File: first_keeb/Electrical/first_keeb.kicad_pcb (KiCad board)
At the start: 2 copper layers, 91.5 x 64.5 mm, 23 parts, among them U1 RPi_Pico_SMD_TH

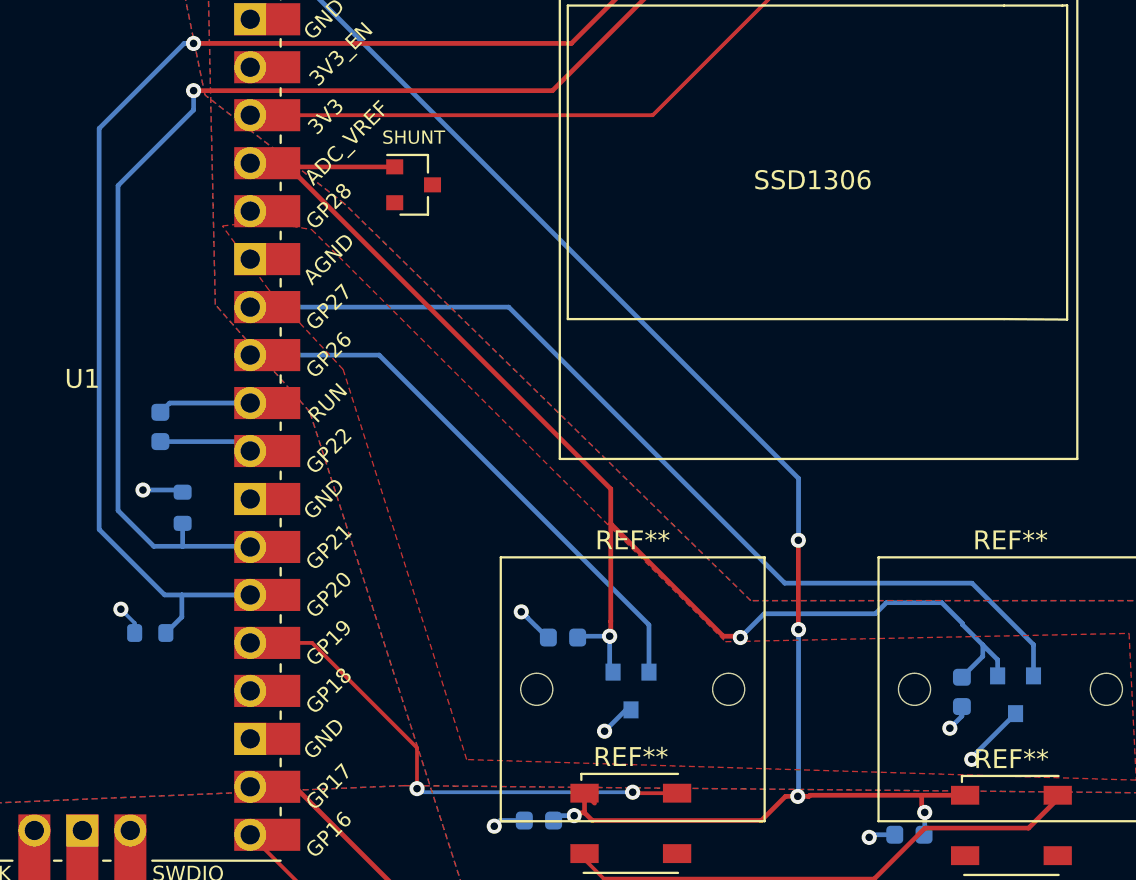
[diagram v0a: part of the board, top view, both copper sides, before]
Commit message: fix ground plane issues
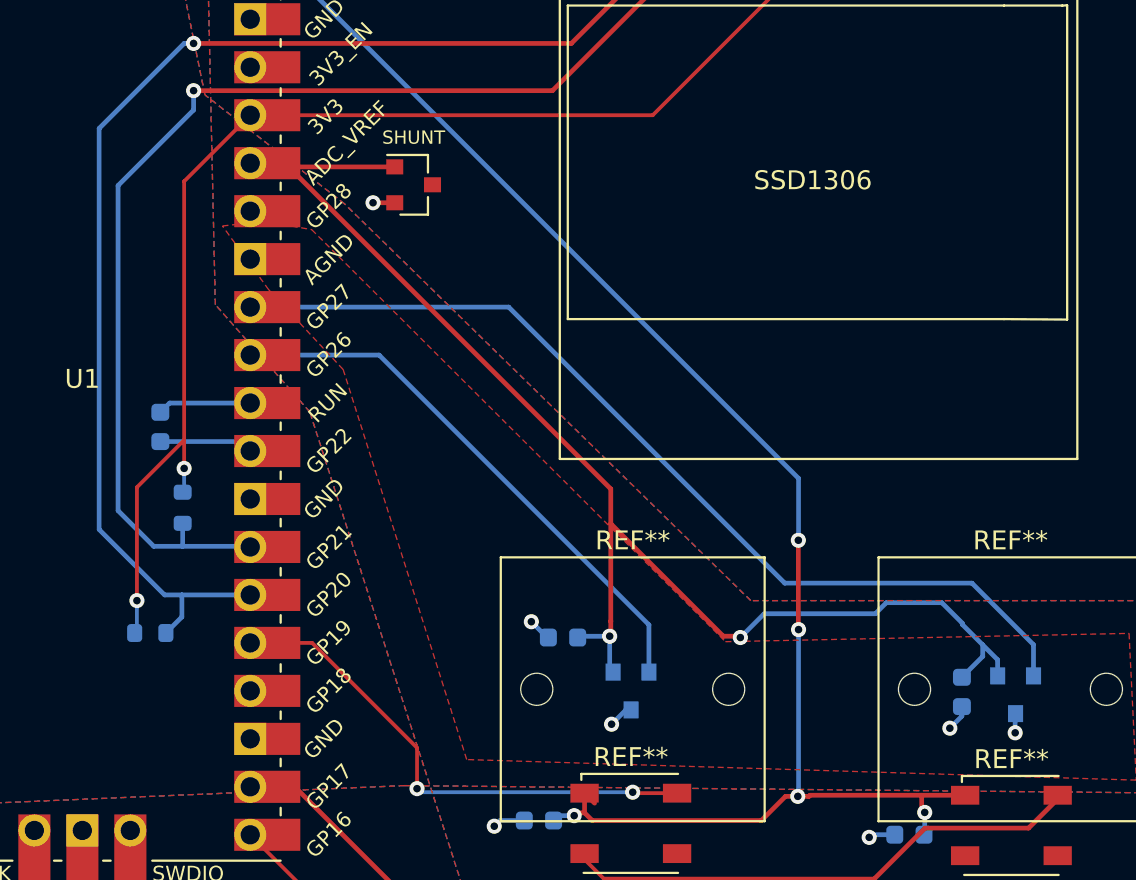
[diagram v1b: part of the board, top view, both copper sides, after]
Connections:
- CUP pad 2: (no net) -> AGND
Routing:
- net (no net): track 559.3 -> 590.6 mm, vias 12 -> 13
- net GND: track 7.09 -> 4.28 mm, vias 4 -> 3
- net AGND: track 7.71 -> 5.30 mm, vias 3 -> 4
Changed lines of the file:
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@@
       (stroke (width 0.1) (type solid)) (layer "B.Fab"))
     (pad "1" smd roundrect (at -0.775 0 270) (size 0.9 0.95) (layers "B.Cu" "B.Paste" "B.Mask") (roundrect_rratio 0.25))
-    (pad "2" smd roundrect (at 0.775 0 270) (size 0.9 0.95) (layers "B.Cu" "B.Paste" "B.Mask") (roundrect_rratio 0.25))
+    (pad "2" smd roundrect (at 0.775 0 270) (size 0.9 0.95) (layers "B.Cu" "B.Paste" "B.Mask") (roundrect_rratio 0.25)
+      (net 1 "AGND"))
     (model "${KICAD6_3DMODEL_DIR}/Capacitor_SMD.3dshapes/C_0603_1608Metric.wrl"
       (offset (xyz 0 0 0))
@@
   (segment (start 86.85 113.805) (end 87.1 113.805) (width 0.2) (layer "F.Cu") (net 0))
   (segment (start 49.195 80.535) (end 56.65 80.535) (width 0.25) (layer "F.Cu") (net 0))
+  (segment (start 45.5 81.3) (end 45.5 95) (width 0.2) (layer "F.Cu") (net 0))
   (segment (start 84.55 114.555) (end 84.71 114.715) (width 0.25) (layer "F.Cu") (net 0))
+  (segment (start 49 77.8) (end 45.5 81.3) (width 0.2) (layer "F.Cu") (net 0))
   (segment (start 84.73 115.545) (end 90.21 115.545) (width 0.25) (layer "F.Cu") (net 0))
   (segment (start 78.64 113.805) (end 84.55 113.805) (width 0.25) (layer "F.Cu") (net 0))
@@
   (segment (start 66 74) (end 72 68) (width 0.25) (layer "F.Cu") (net 0))
   (segment (start 78.03 105.035) (end 78.02 105.045) (width 0.25) (layer "F.Cu") (net 0))
+  (segment (start 45.5 95) (end 45.5 96.5) (width 0.2) (layer "F.Cu") (net 0))
   (segment (start 66.7 117.205) (end 67.74 118.245) (width 0.2) (layer "F.Cu") (net 0))
   (segment (start 69.25 113.645) (end 69.3 113.695) (width 0.2) (layer "F.Cu") (net 0))
@@
   (segment (start 67.74 118.245) (end 82.03 118.245) (width 0.25) (layer "F.Cu") (net 0))
   (segment (start 57.83 111.295) (end 52.275 105.74) (width 0.2) (layer "F.Cu") (net 0))
+  (segment (start 43 97.5) (end 43 103.5) (width 0.2) (layer "F.Cu") (net 0))
   (segment (start 78.02 100.305) (end 78.02 105.025) (width 0.25) (layer "F.Cu") (net 0))
   (segment (start 77.99 113.865) (end 77.34 113.865) (width 0.25) (layer "F.Cu") (net 0))
@@
   (segment (start 49 77.8) (end 70.31 77.8) (width 0.2) (layer "F.Cu") (net 0))
   (segment (start 69.3 113.695) (end 71.6 113.695) (width 0.2) (layer "F.Cu") (net 0))
+  (segment (start 45.5 95) (end 43 97.5) (width 0.2) (layer "F.Cu") (net 0))
   (segment (start 68.09 104.585) (end 68.09 105.325) (width 0.25) (layer "F.Cu") (net 0))
   (segment (start 76.06 115.145) (end 67.11 115.145) (width 0.25) (layer "F.Cu") (net 0))
@@
   (via (at 78.03 105.035) (size 0.8) (drill 0.4) (layers "F.Cu" "B.Cu") (net 0))
   (via (at 84.71 114.715) (size 0.8) (drill 0.4) (layers "F.Cu" "B.Cu") (net 0))
+  (via (at 45.5 96.5) (size 0.8) (drill 0.4) (layers "F.Cu" "B.Cu") (net 0))
   (via (at 78.02 100.305) (size 0.8) (drill 0.4) (layers "F.Cu" "B.Cu") (net 0))
-  (via (at 86.04 110.255) (size 0.8) (drill 0.4) (layers "F.Cu" "B.Cu") (net 0))
+  (via (at 43 103.5) (size 0.8) (drill 0.4) (layers "F.Cu" "B.Cu") (free) (net 0))
   (via (at 77.99 113.865) (size 0.8) (drill 0.4) (layers "F.Cu" "B.Cu") (net 0))
   (via (at 66.15 114.885) (size 0.8) (drill 0.4) (layers "F.Cu" "B.Cu") (net 0))
@@
   (segment (start 86.7 104.765) (end 86.7 104.695) (width 0.25) (layer "B.Cu") (net 0))
   (segment (start 78.02 100.305) (end 78.03 100.295) (width 0.25) (layer "B.Cu") (net 0))
-  (segment (start 86.68 109.615) (end 86.04 110.255) (width 0.25) (layer "B.Cu") (net 0))
   (segment (start 70.11 107.285) (end 70.11 104.785) (width 0.25) (layer "B.Cu") (net 0))
   (segment (start 41 99.735) (end 41 78.5) (width 0.25) (layer "B.Cu") (net 0))
@@
   (segment (start 76.21 104.195) (end 74.95 105.455) (width 0.25) (layer "B.Cu") (net 0))
   (segment (start 41 78.5) (end 45.5 74) (width 0.25) (layer "B.Cu") (net 0))
+  (segment (start 43 105.095) (end 42.88 105.215) (width 0.2) (layer "B.Cu") (net 0))
   (segment (start 49 93.04) (end 44.73 93.04) (width 0.25) (layer "B.Cu") (net 0))
+  (segment (start 43 103.5) (end 43 105.095) (width 0.2) (layer "B.Cu") (net 0))
   (segment (start 68.03 105.385) (end 66.405 105.385) (width 0.25) (layer "B.Cu") (net 0))
   (segment (start 69.25 113.645) (end 58.02 113.645) (width 0.2) (layer "B.Cu") (net 0))
@@
   (segment (start 66.405 105.385) (end 66.335 105.455) (width 0.25) (layer "B.Cu") (net 0))
   (segment (start 84.71 114.715) (end 84.71 115.86) (width 0.25) (layer "B.Cu") (net 0))
+  (segment (start 45.5 97.68) (end 45.42 97.76) (width 0.2) (layer "B.Cu") (net 0))
   (segment (start 88.57 107.485) (end 88.57 106.635) (width 0.25) (layer "B.Cu") (net 0))
   (segment (start 87.785 105.85) (end 87.785 106.455) (width 0.25) (layer "B.Cu") (net 0))
+  (segment (start 45.5 96.5) (end 45.5 97.68) (width 0.2) (layer "B.Cu") (net 0))
   (segment (start 58.02 113.645) (end 57.83 113.455) (width 0.2) (layer "B.Cu") (net 0))
   (segment (start 52.355 71.355) (end 50.175 71.355) (width 0.25) (layer "B.Cu") (net 0))
@@
   (segment (start 82.094695 104.195) (end 76.21 104.195) (width 0.25) (layer "B.Cu") (net 0))
   (segment (start 68.03 105.385) (end 68.03 107.105) (width 0.25) (layer "B.Cu") (net 0))
-  (segment (start 86.68 109.11) (end 86.68 109.615) (width 0.25) (layer "B.Cu") (net 0))
   (segment (start 88.57 106.635) (end 87.785 105.85) (width 0.25) (layer "B.Cu") (net 0))
   (segment (start 78.03 105.035) (end 78.03 113.825) (width 0.25) (layer "B.Cu") (net 0))
   (segment (start 45.38 103.2) (end 44.465 103.2) (width 0.25) (layer "B.Cu") (net 0))
   (segment (start 78.03 113.825) (end 77.99 113.865) (width 0.25) (layer "B.Cu") (net 0))
-  (via (at 63.35 104.095) (size 0.8) (drill 0.4) (layers "F.Cu" "B.Cu") (net 1))
-  (via (at 87.2 111.905) (size 0.8) (drill 0.4) (layers "F.Cu" "B.Cu") (free) (net 1))
-  (via (at 67.76 110.415) (size 0.8) (drill 0.4) (layers "F.Cu" "B.Cu") (free) (net 1))
-  (segment (start 69.16 109.285) (end 68.89 109.285) (width 0.25) (layer "B.Cu") (net 1))
-  (segment (start 87.2 111.905) (end 87.2 111.805) (width 0.25) (layer "B.Cu") (net 1))
-  (segment (start 64.785 105.455) (end 64.74 105.455) (width 0.25) (layer "B.Cu") (net 1))
-  (segment (start 64.74 105.455) (end 63.35 104.095) (width 0.25) (layer "B.Cu") (net 1))
-  (segment (start 87.2 111.805) (end 89.52 109.485) (width 0.25) (layer "B.Cu") (net 1))
-  (segment (start 63.35 104.095) (end 63.7 104.415) (width 0.25) (layer "B.Cu") (net 1))
-  (segment (start 68.89 109.285) (end 67.76 110.415) (width 0.25) (layer "B.Cu") (net 1))
-  (segment (start 43.17 97.495) (end 43.32 97.645) (width 0.25) (layer "F.Cu") (net 2))
-  (segment (start 42.12 103.925) (end 42.15 103.955) (width 0.25) (layer "F.Cu") (net 2))
+  (via (at 63.883255 104.616745) (size 0.8) (drill 0.4) (layers "F.Cu" "B.Cu") (net 1))
+  (via (at 89.5 110.5) (size 0.8) (drill 0.4) (layers "F.Cu" "B.Cu") (free) (net 1))
+  (via (at 68.13 110.045) (size 0.8) (drill 0.4) (layers "F.Cu" "B.Cu") (free) (net 1))
+  (via (at 86.04 110.255) (size 0.8) (drill 0.4) (layers "F.Cu" "B.Cu") (net 1))
+  (segment (start 63.883255 104.616745) (end 64.72151 105.455) (width 0.25) (layer "B.Cu") (net 1))
+  (segment (start 86.68 109.615) (end 86.04 110.255) (width 0.25) (layer "B.Cu") (net 1))
+  (segment (start 68.13 110.045) (end 68.89 109.285) (width 0.25) (layer "B.Cu") (net 1))
+  (segment (start 63.883255 104.616745) (end 63.883255 104.598255) (width 0.25) (layer "B.Cu") (net 1))
+  (segment (start 89.5 110.5) (end 89.5 109.505) (width 0.25) (layer "B.Cu") (net 1))
+  (segment (start 63.883255 104.598255) (end 63.7 104.415) (width 0.25) (layer "B.Cu") (net 1))
+  (segment (start 68.89 109.285) (end 69.16 109.285) (width 0.25) (layer "B.Cu") (net 1))
+  (segment (start 64.72151 105.455) (end 64.785 105.455) (width 0.25) (layer "B.Cu") (net 1))
+  (segment (start 89.5 109.505) (end 89.52 109.485) (width 0.25) (layer "B.Cu") (net 1))
+  (segment (start 86.68 109.11) (end 86.68 109.615) (width 0.25) (layer "B.Cu") (net 1))
+  (segment (start 55.5 82.435) (end 56.65 82.435) (width 0.25) (layer "F.Cu") (net 2))
+  (via (at 55.5 82.435) (size 0.8) (drill 0.4) (layers "F.Cu" "B.Cu") (free) (net 2))
   (via (at 81.77 116.035) (size 0.8) (drill 0.4) (layers "F.Cu" "B.Cu") (net 2))
-  (via (at 42.15 103.955) (size 0.8) (drill 0.4) (layers "F.Cu" "B.Cu") (net 2))
-  (via (at 43.32 97.645) (size 0.8) (drill 0.4) (layers "F.Cu" "B.Cu") (net 2))
   (via (at 61.92 115.445) (size 0.8) (drill 0.4) (layers "F.Cu" "B.Cu") (net 2))
-  (segment (start 45.305 97.645) (end 45.42 97.76) (width 0.25) (layer "B.Cu") (net 2))
-  (segment (start 43.32 97.645) (end 45.305 97.645) (width 0.25) (layer "B.Cu") (net 2))
-  (segment (start 42.88 104.685) (end 42.15 103.955) (width 0.2) (layer "B.Cu") (net 2))
-  (segment (start 42.88 105.215) (end 42.88 104.685) (width 0.2) (layer "B.Cu") (net 2))
   (segment (start 63.51 115.145) (end 62.22 115.145) (width 0.25) (layer "B.Cu") (net 2))
   (segment (start 83.125 115.895) (end 81.91 115.895) (width 0.25) (layer "B.Cu") (net 2))
@@
     (connect_pads (clearance 0.508))
     (min_thickness 0.25) (filled_areas_thickness no)
-    (fill yes (thermal_gap 0.5) (thermal_bridge_width 0.5) (island_removal_mode 1) (island_area_min 10))
+    (fill yes (thermal_gap 0.5) (thermal_bridge_width 0.5))
     (polygon
       (pts

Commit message: remove unused via to gnd
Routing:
- net GND: track 4.28 -> 1.15 mm, vias 3 -> 1
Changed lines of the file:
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@@
   (segment (start 55.5 82.435) (end 56.65 82.435) (width 0.25) (layer "F.Cu") (net 2))
   (via (at 55.5 82.435) (size 0.8) (drill 0.4) (layers "F.Cu" "B.Cu") (free) (net 2))
-  (via (at 81.77 116.035) (size 0.8) (drill 0.4) (layers "F.Cu" "B.Cu") (net 2))
-  (via (at 61.92 115.445) (size 0.8) (drill 0.4) (layers "F.Cu" "B.Cu") (net 2))
-  (segment (start 63.51 115.145) (end 62.22 115.145) (width 0.25) (layer "B.Cu") (net 2))
-  (segment (start 83.125 115.895) (end 81.91 115.895) (width 0.25) (layer "B.Cu") (net 2))
-  (segment (start 62.22 115.145) (end 61.92 115.445) (width 0.25) (layer "B.Cu") (net 2))
-  (segment (start 81.91 115.895) (end 81.77 116.035) (width 0.25) (layer "B.Cu") (net 2))
   (zone (net 1) (net_name "AGND") (layer "F.Cu") (hatch edge 0.5)
     (connect_pads (clearance 0.508))

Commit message: actual v1
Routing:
- net (no net): track 590.6 -> 593.3 mm
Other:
- board text added: "Sensors connected to 3V3"
